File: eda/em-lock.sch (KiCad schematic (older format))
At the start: 48 parts

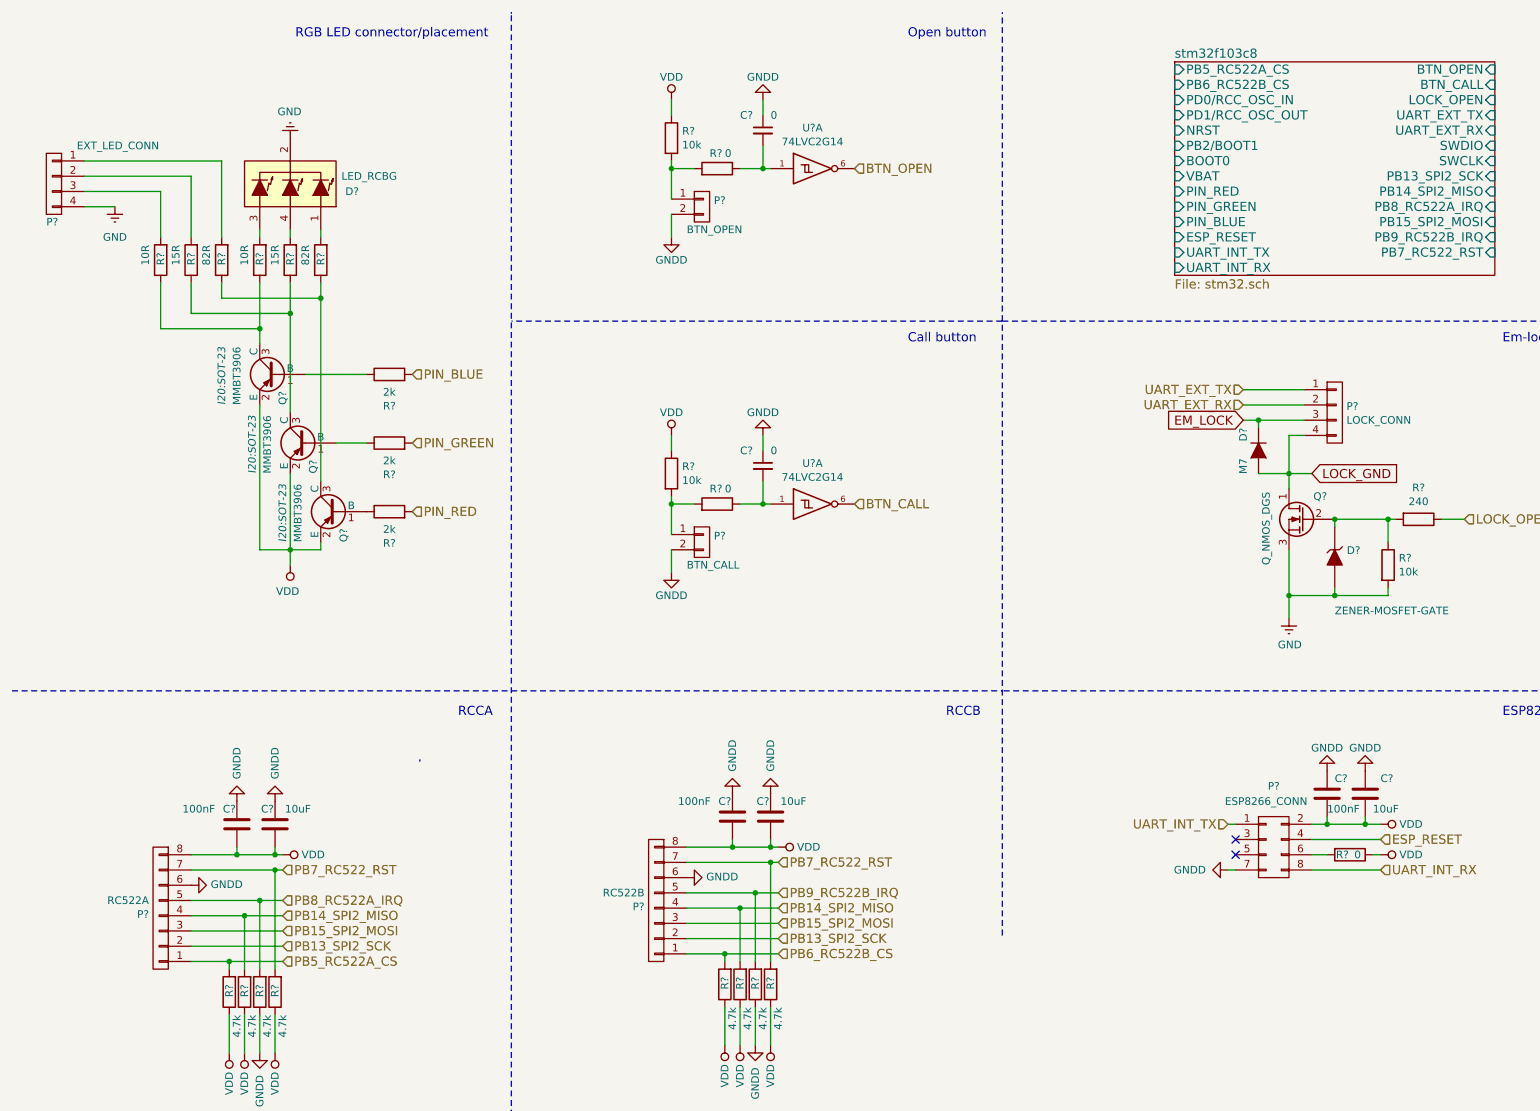
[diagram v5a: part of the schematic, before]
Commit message: refs #41563 fix stable schematics version
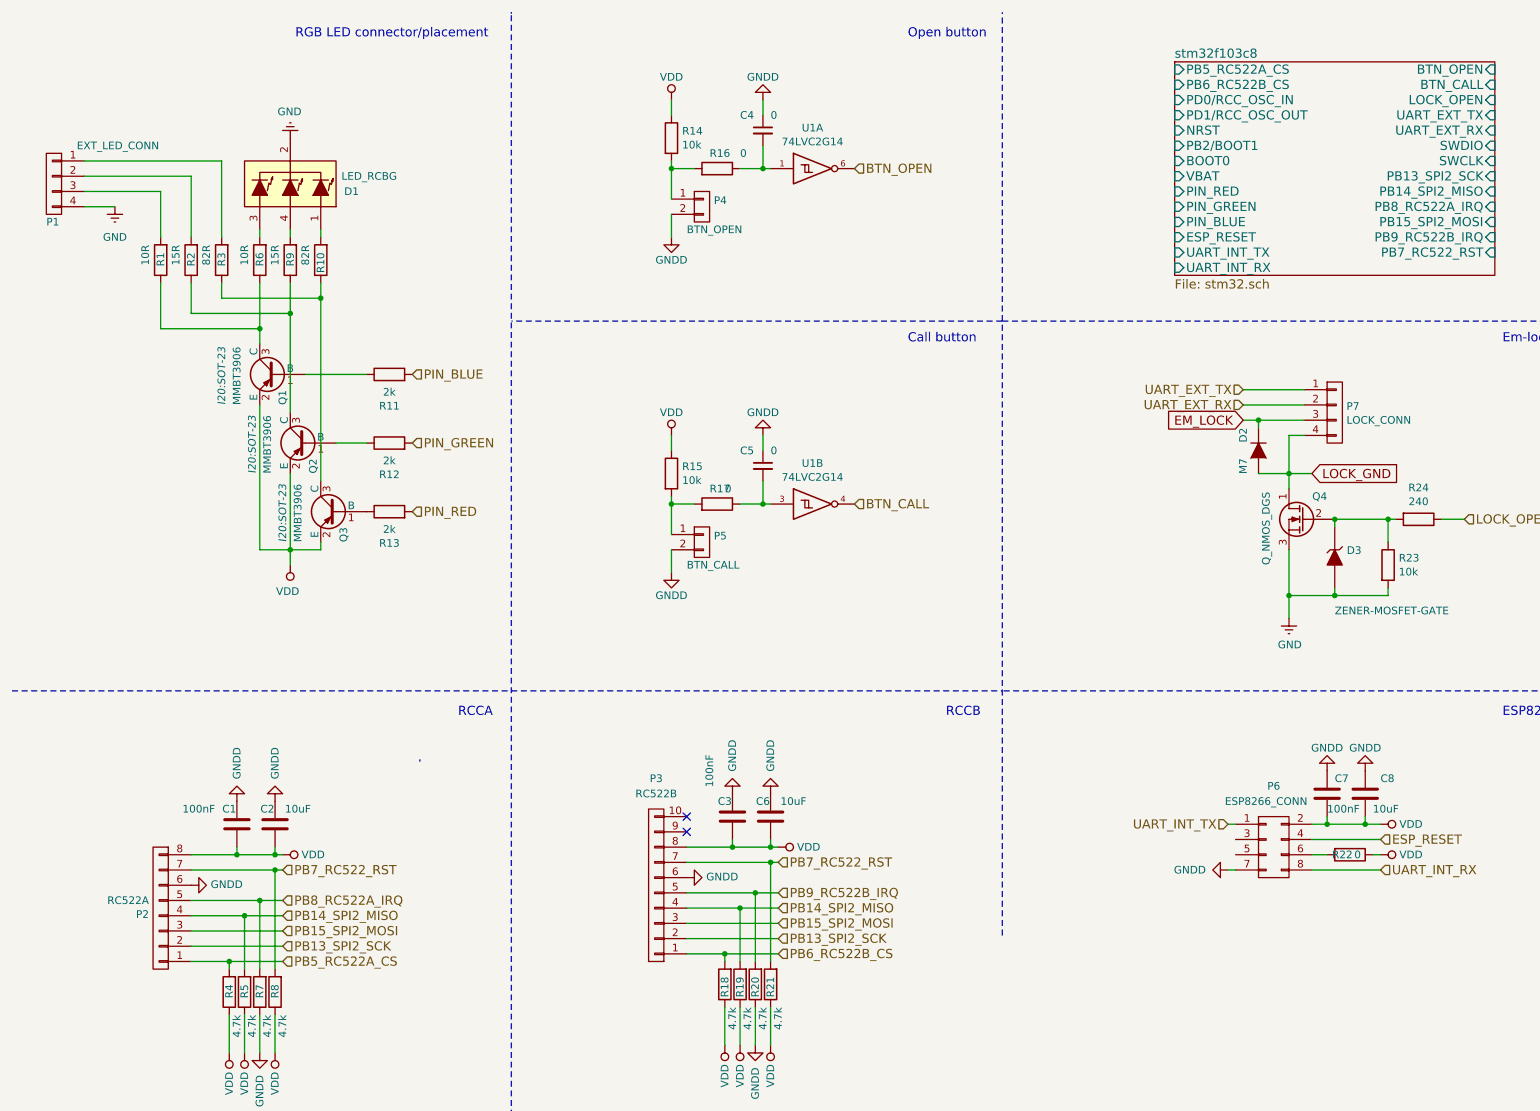
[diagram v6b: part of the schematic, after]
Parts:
- removed P?: RC522B, symbol CONN_01X08
- added P3: RC522B, Pin_Headers:Pin_Header_Straight_2x05, symbol CONN_01X10
- C1, C2, C3, C6, C7, C8: renamed from C?; footprint I20:C_0805_HandSoldering -> I20:C_0805
- C4, C5: renamed from C?; footprint (none) -> I20:C_0805
- P2: renamed from P?; footprint (none) -> Pin_Headers:Pin_Header_Straight_1x08
- gave numbers to parts that had none: 37
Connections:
- net BTN_CALL: now also U1.4; no longer U1.6
- net GNDD: now also P3.6 (P6)
- net PB13_SPI2_SCK: now also P3.2 (P2)
- net PB14_SPI2_MISO: now also P3.4 (P4)
- net PB15_SPI2_MOSI: now also P3.3 (P3)
- net PB6_RC522B_CS: now also P3.1 (P1)
- net PB7_RC522_RST: now also P3.7 (P7)
- net PB9_RC522B_IRQ: now also P3.5 (P5)
- net VDD: now also P3.8 (P8)
- net at C5.2, R17.1: now also U1.3; no longer U1.1

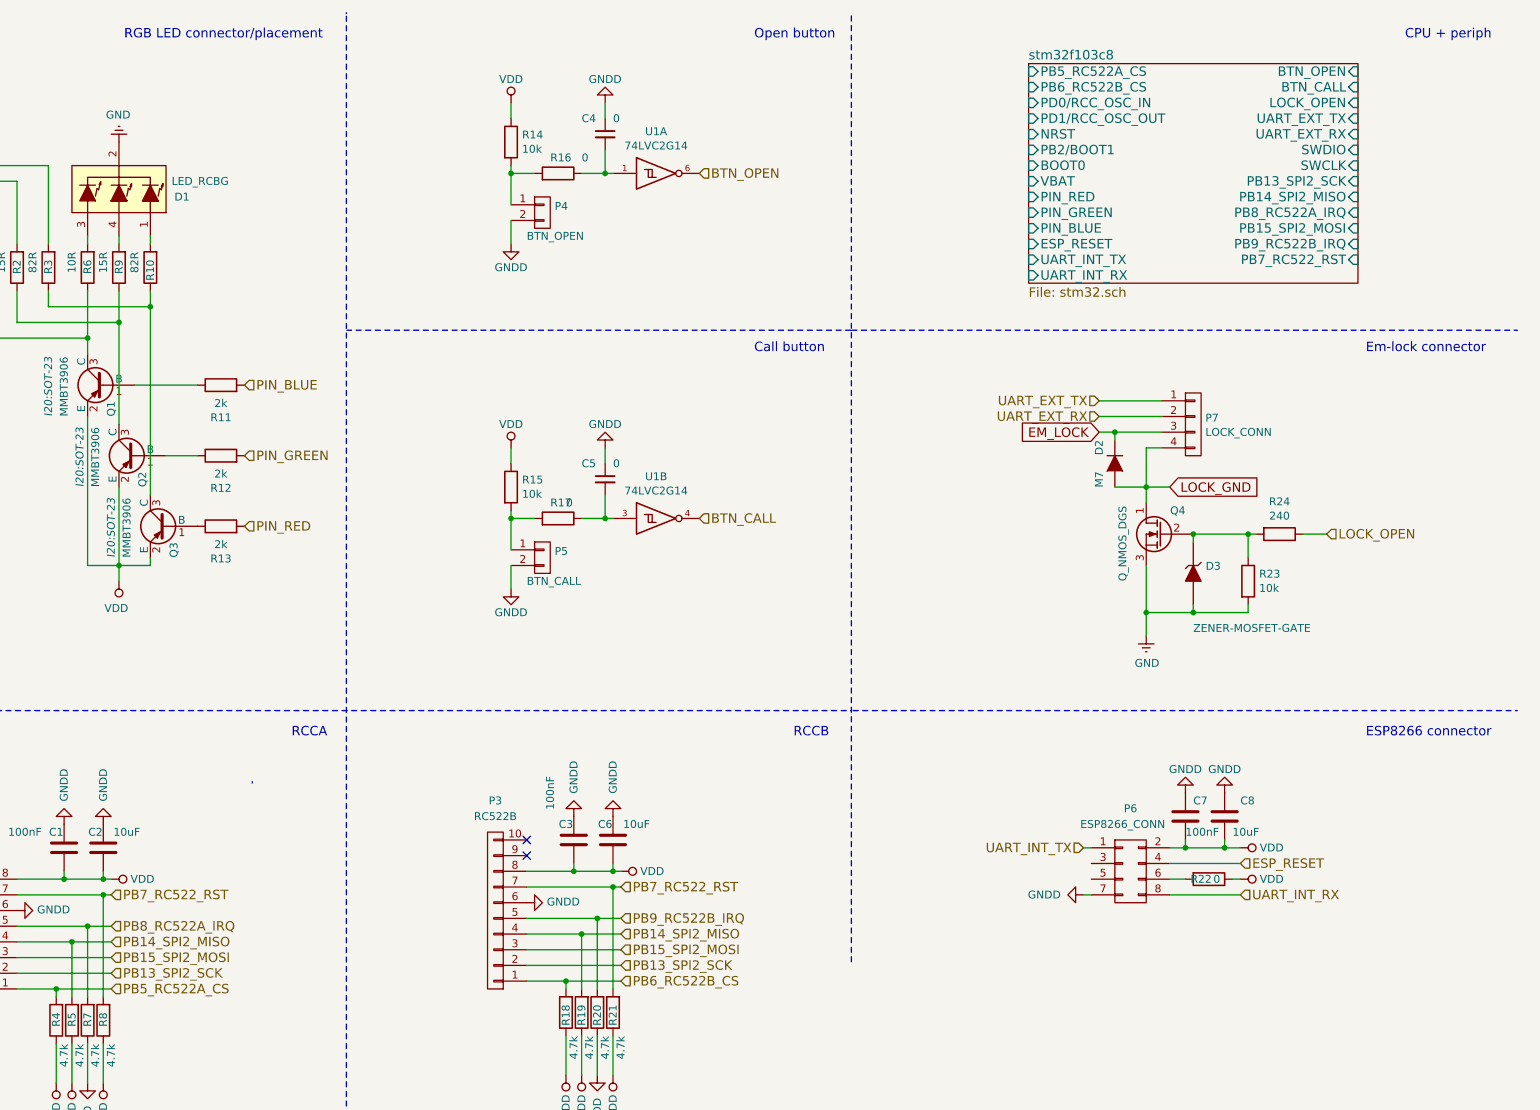
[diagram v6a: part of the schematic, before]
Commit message: refs #41563 pcb projecting half-done
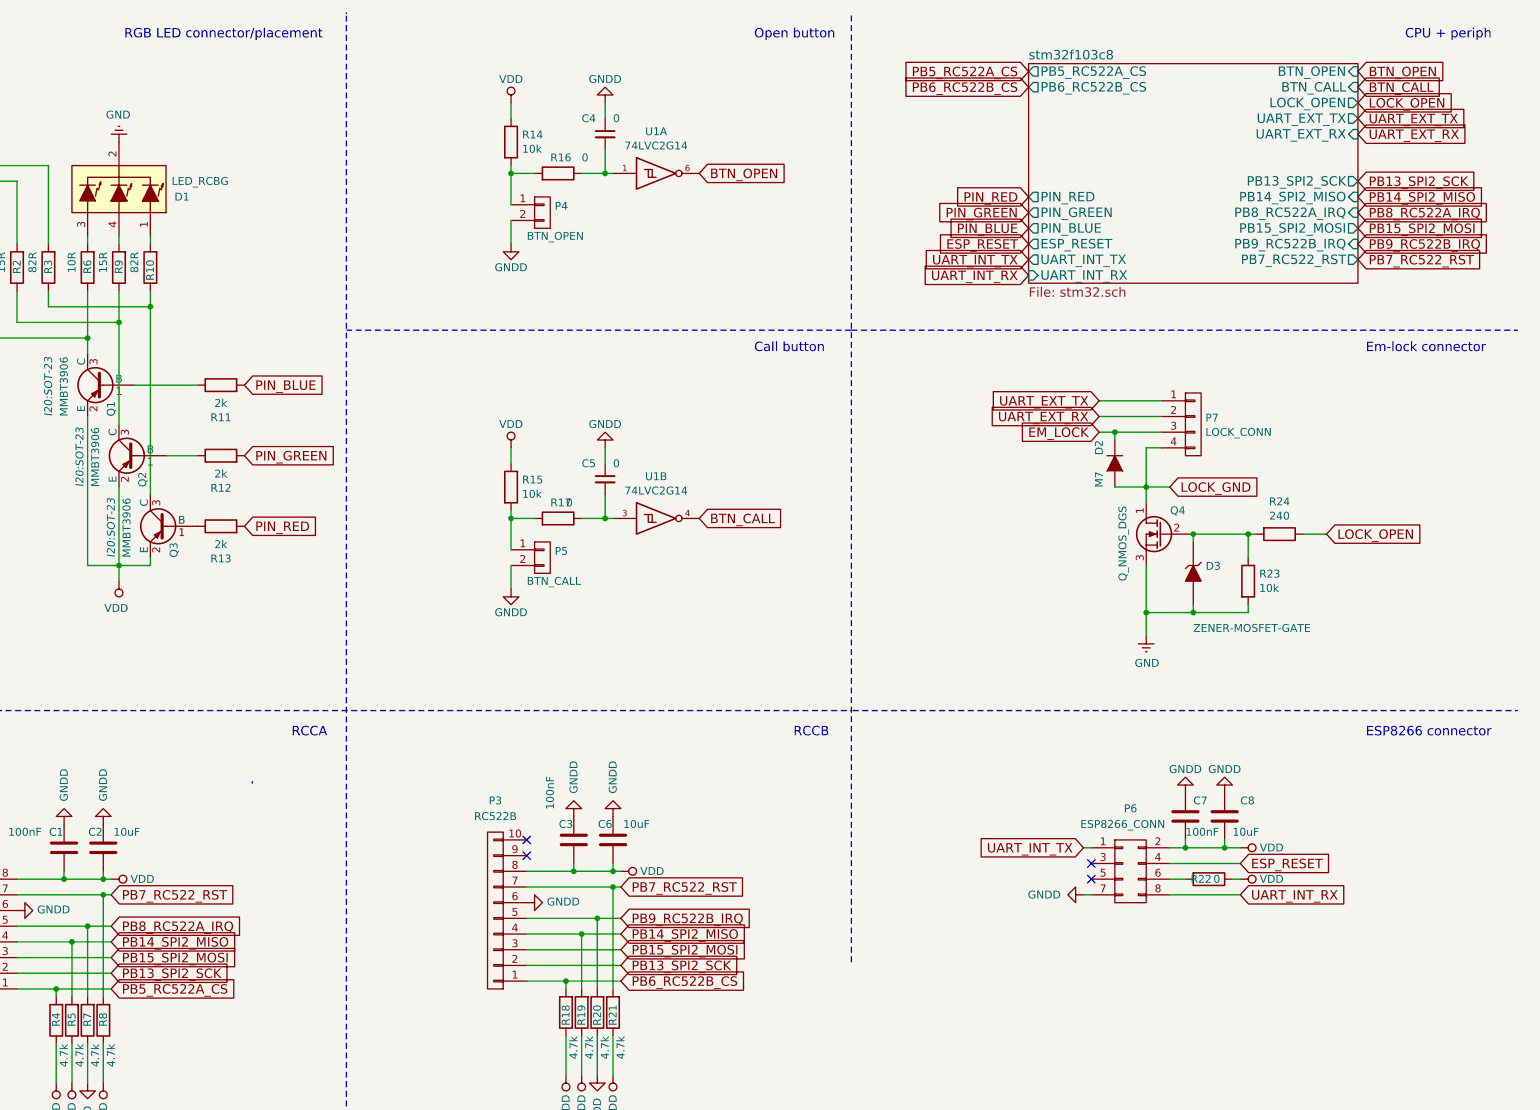
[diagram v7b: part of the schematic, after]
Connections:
- no-connect marks 2 -> 4
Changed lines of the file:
@@
 F0 "stm32f103c8" 60
 F1 "stm32.sch" 60
-F2 "PD0/RCC_OSC_IN" I L 8100 1050 60
-F3 "PD1/RCC_OSC_OUT" I L 8100 1150 60
-F4 "NRST" I L 8100 1250 60
-F5 "PB2/BOOT1" I L 8100 1350 60
-F6 "BOOT0" I L 8100 1450 60
-F7 "VBAT" I L 8100 1550 60
-F8 "PIN_RED" I L 8100 1650 60
-F9 "PIN_GREEN" I L 8100 1750 60
-F10 "PIN_BLUE" I L 8100 1850 60
-F11 "ESP_RESET" I L 8100 1950 60
-F12 "UART_INT_TX" I L 8100 2050 60
-F13 "UART_INT_RX" I L 8100 2150 60
-F14 "BTN_OPEN" I R 10200 850 60
-F15 "BTN_CALL" I R 10200 950 60
-F16 "LOCK_OPEN" I R 10200 1050 60
-F17 "UART_EXT_TX" I R 10200 1150 60
-F18 "UART_EXT_RX" I R 10200 1250 60
-F19 "SWDIO" I R 10200 1350 60
-F20 "SWCLK" I R 10200 1450 60
-F21 "PB13_SPI2_SCK" I R 10200 1550 60
-F22 "PB14_SPI2_MISO" I R 10200 1650 60
-F23 "PB15_SPI2_MOSI" I R 10200 1850 60
-F24 "PB8_RC522A_IRQ" I R 10200 1750 60
-F25 "PB9_RC522B_IRQ" I R 10200 1950 60
-F26 "PB7_RC522_RST" I R 10200 2050 60
-F27 "PB5_RC522A_CS" I L 8100 850 60
-F28 "PB6_RC522B_CS" I L 8100 950 60
+F2 "PIN_RED" O L 8100 1650 60
+F3 "PIN_GREEN" O L 8100 1750 60
+F4 "PIN_BLUE" O L 8100 1850 60
+F5 "ESP_RESET" O L 8100 1950 60
+F6 "UART_INT_TX" O L 8100 2050 60
+F7 "UART_INT_RX" I L 8100 2150 60
+F8 "BTN_OPEN" I R 10200 850 60
+F9 "BTN_CALL" I R 10200 950 60
+F10 "LOCK_OPEN" O R 10200 1050 60
+F11 "UART_EXT_TX" O R 10200 1150 60
+F12 "UART_EXT_RX" I R 10200 1250 60
+F13 "PB13_SPI2_SCK" O R 10200 1550 60
+F14 "PB14_SPI2_MISO" I R 10200 1650 60
+F15 "PB15_SPI2_MOSI" O R 10200 1850 60
+F16 "PB8_RC522A_IRQ" I R 10200 1750 60
+F17 "PB9_RC522B_IRQ" I R 10200 1950 60
+F18 "PB7_RC522_RST" O R 10200 2050 60
+F19 "PB5_RC522A_CS" O L 8100 850 60
+F20 "PB6_RC522B_CS" O L 8100 950 60
 $EndSheet
-Text HLabel 3100 3750 2    60   Input ~ 0
+Text GLabel 3100 3750 2    60   Input ~ 0
 PIN_RED
-Text HLabel 3100 3300 2    60   Input ~ 0
+Text GLabel 3100 3300 2    60   Input ~ 0
 PIN_GREEN
-Text HLabel 3100 2850 2    60   Input ~ 0
+Text GLabel 3100 2850 2    60   Input ~ 0
 PIN_BLUE
-Text HLabel 9450 5900 2    60   Input ~ 0
+Text GLabel 9450 5900 2    60   Input ~ 0
 ESP_RESET
-Text HLabel 8450 5800 0    60   Input ~ 0
+Text GLabel 8450 5800 0    60   Input ~ 0
 UART_INT_TX
-Text HLabel 10000 3800 2    60   Input ~ 0
+Text GLabel 10000 3800 2    60   Input ~ 0
 LOCK_OPEN
-Text HLabel 8550 2950 0    60   Input ~ 0
+Text GLabel 8550 2950 0    60   Input ~ 0
 UART_EXT_TX
-Text HLabel 8550 3050 0    60   Input ~ 0
+Text GLabel 8550 3050 0    60   Input ~ 0
 UART_EXT_RX
-Text HLabel 6000 3700 2    60   Input ~ 0
+Text GLabel 6000 3700 2    60   Input ~ 0
 BTN_CALL
 Text Notes 3600 650  2    60   ~ 0
@@
 	-1   0    0    1
 $EndComp
-Text HLabel 2250 6700 2    60   Input ~ 0
+Text GLabel 2250 6700 2    60   Input ~ 0
 PB5_RC522A_CS
-Text HLabel 2250 6600 2    60   Input ~ 0
+Text GLabel 2250 6600 2    60   Input ~ 0
 PB13_SPI2_SCK
-Text HLabel 2250 6400 2    60   Input ~ 0
+Text GLabel 2250 6400 2    60   Input ~ 0
 PB14_SPI2_MISO
-Text HLabel 2250 6500 2    60   Input ~ 0
+Text GLabel 2250 6500 2    60   Input ~ 0
 PB15_SPI2_MOSI
-Text HLabel 2250 6300 2    60   Input ~ 0
+Text GLabel 2250 6300 2    60   Input ~ 0
 PB8_RC522A_IRQ
-Text HLabel 2250 6100 2    60   Input ~ 0
+Text GLabel 2250 6100 2    60   Input ~ 0
 PB7_RC522_RST
 $Comp
@@
 	1    0    0    -1
 $EndComp
-Text HLabel 6000 1500 2    60   Input ~ 0
+Text GLabel 6000 1500 2    60   Input ~ 0
 BTN_OPEN
 $Comp
@@
 	-1   0    0    1
 $EndComp
-Text HLabel 5500 6550 2    60   Input ~ 0
+Text GLabel 5500 6550 2    60   Input ~ 0
 PB13_SPI2_SCK
-Text HLabel 5500 6350 2    60   Input ~ 0
+Text GLabel 5500 6350 2    60   Input ~ 0
 PB14_SPI2_MISO
-Text HLabel 5500 6450 2    60   Input ~ 0
+Text GLabel 5500 6450 2    60   Input ~ 0
 PB15_SPI2_MOSI
-Text HLabel 5500 6250 2    60   Input ~ 0
+Text GLabel 5500 6250 2    60   Input ~ 0
 PB9_RC522B_IRQ
-Text HLabel 5500 6050 2    60   Input ~ 0
+Text GLabel 5500 6050 2    60   Input ~ 0
 PB7_RC522_RST
 $Comp
@@
 	0    1    1    0
 $EndComp
-Text HLabel 5500 6650 2    60   Input ~ 0
+Text GLabel 5500 6650 2    60   Input ~ 0
 PB6_RC522B_CS
 Text GLabel 9000 3500 2    60   Input ~ 0
@@
 Wire Wire Line
 	9400 6000 9450 6000
-Text HLabel 9450 6100 2    60   Input ~ 0
+Text GLabel 9450 6100 2    60   Input ~ 0
 UART_INT_RX
+Text GLabel 8100 850  0    60   Input ~ 0
+PB5_RC522A_CS
+Text GLabel 10200 1550 2    60   Input ~ 0
+PB13_SPI2_SCK
+Text GLabel 10200 1650 2    60   Input ~ 0
+PB14_SPI2_MISO
+Text GLabel 10200 1850 2    60   Input ~ 0
+PB15_SPI2_MOSI
+Text GLabel 10200 1750 2    60   Input ~ 0
+PB8_RC522A_IRQ
+Text GLabel 10200 2050 2    60   Input ~ 0
+PB7_RC522_RST
+Text GLabel 10200 1150 2    60   Input ~ 0
+UART_EXT_TX
+Text GLabel 10200 1250 2    60   Input ~ 0
+UART_EXT_RX
+Text GLabel 10200 1050 2    60   Input ~ 0
+LOCK_OPEN
+Text GLabel 8100 1950 0    60   Input ~ 0
+ESP_RESET
+Text GLabel 8100 2150 0    60   Input ~ 0
+UART_INT_RX
+Text GLabel 8100 2050 0    60   Input ~ 0
+UART_INT_TX
+Text GLabel 10200 1950 2    60   Input ~ 0
+PB9_RC522B_IRQ
+Text GLabel 8100 950  0    60   Input ~ 0
+PB6_RC522B_CS
+Text GLabel 10200 850  2    60   Input ~ 0
+BTN_OPEN
+Text GLabel 10200 950  2    60   Input ~ 0
+BTN_CALL
+Text GLabel 8100 1850 0    60   Input ~ 0
+PIN_BLUE
+Text GLabel 8100 1750 0    60   Input ~ 0
+PIN_GREEN
+Text GLabel 8100 1650 0    60   Input ~ 0
+PIN_RED
+NoConn ~ 8500 6000
+NoConn ~ 8500 5900
 $EndSCHEMATC
